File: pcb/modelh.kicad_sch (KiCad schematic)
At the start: 41 parts, among them J1 Battery Conn, J2 Conn_01x20, J3 Conn_01x06, J4 Conn_01x12, J5 Conn_01x04, SW1 SW_reset, U1 nice_nano, U2 74HC595, U3 74HC595, U4 74HC595

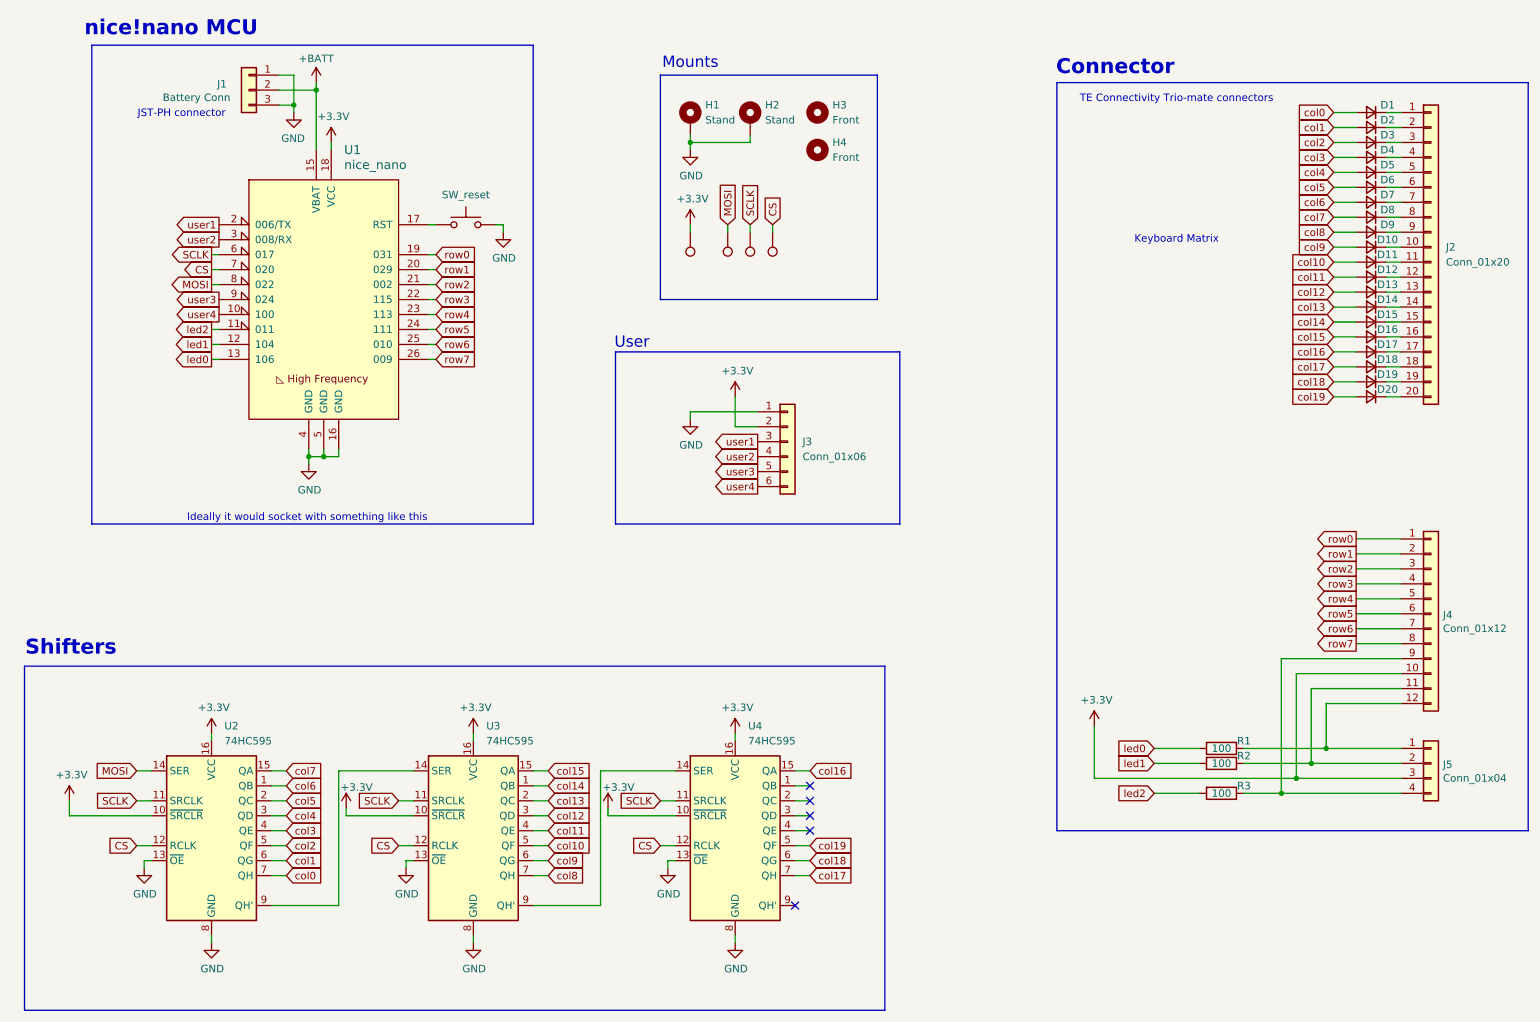
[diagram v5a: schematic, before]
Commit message: Aligned connectors correctly, added second 4 pin footprint
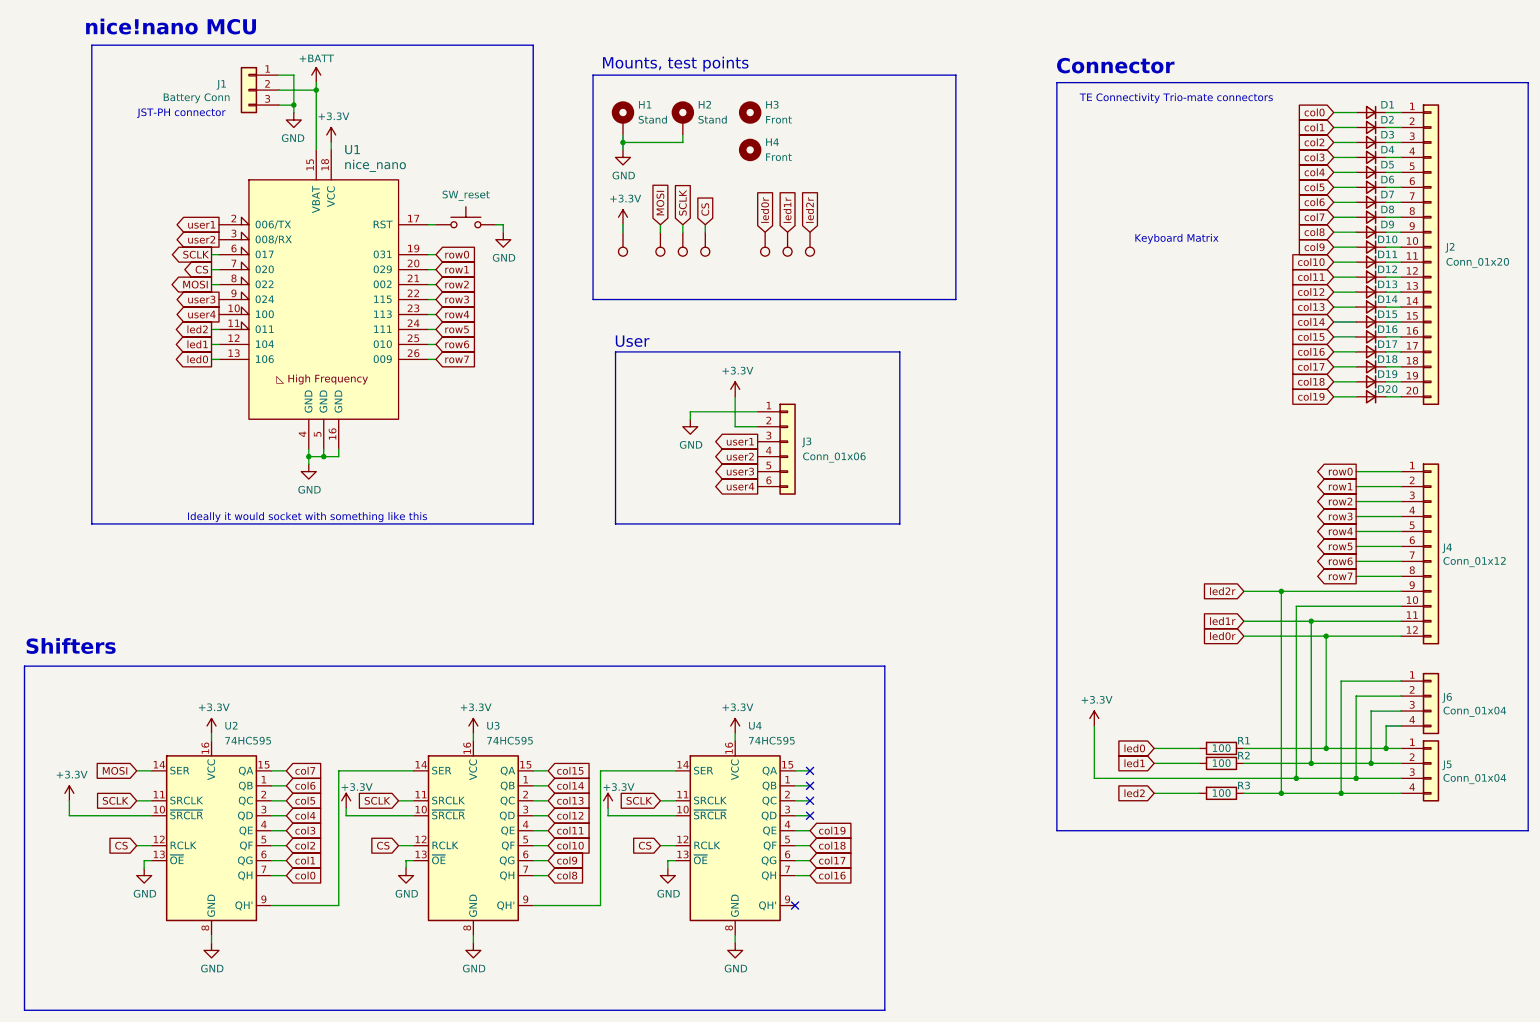
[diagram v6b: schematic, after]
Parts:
- added J6: Conn_01x04, Library:ModelH-triomate-leds4, symbol Connector_Generic:Conn_01x04
- added TP5: LED1, Library:TestPoint, symbol Connector:TestPoint
- added TP6: LED2, Library:TestPoint, symbol Connector:TestPoint
- added TP7: LED3, Library:TestPoint, symbol Connector:TestPoint
- D1, D10, D11, D12, D13, D14, D15, D16, D17, D18, D19, D2, D20, D3, D4, D5, D6, D7, D8, D9: footprint Diode_SMD:D_SOD-123F -> Library:DO-35 smaller
- J1: footprint Connector_JST:JST_PH_S3B-PH-K_1x03_P2.00mm_Horizontal -> Connector_JST:JST_PH_B3B-PH-K_1x03_P2.00mm_Vertical
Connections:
- net +3.3V: now also J6.2 (Pin_2)
- net GND: now also SW1.1; no longer SW1.2
- net col16: now also U4.7 (QH); no longer U4.15 (QA)
- net col17: now also U4.6 (QG); no longer U4.7 (QH)
- net col18: now also U4.5 (QF); no longer U4.6 (QG)
- net col19: now also U4.4 (QE); no longer U4.5 (QF)
- net led0r: now reaches J4.12 (Pin_12), J5.1 (Pin_1), R1.1
- net led0r: now also J6.4 (Pin_4), TP5.1
- net led1r: now reaches J4.11 (Pin_11), J5.2 (Pin_2), R2.1
- net led1r: now also J6.3 (Pin_3), TP6.1
- net led2r: now reaches J4.9 (Pin_9), J5.4 (Pin_4), R3.1
- net led2r: now also J6.1 (Pin_1), TP7.1
- net at U1.17 (RST): now also SW1.2; no longer SW1.1
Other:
- note added: "Mounts, test points"
- note removed: "Mounts"
- moved on the sheet: H1, H2, H3, H4, J4

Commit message: Added testpad labels, ibom
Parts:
- TP5: value LED1 -> LED0
- TP6: value LED2 -> LED1
- TP7: value LED3 -> LED2
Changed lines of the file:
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@@
 			)
 		)
-		(property "Datasheet" "~"
+		(property "Datasheet" "https://42keebs.eu/shop/parts/components/reset-switch/?attribute_type=Through-hole%202-pin%206x3&attribute_pa_colour=black"
 			(at 96.52 52.07 0)
 			(effects
@@
 			)
 		)
-		(property "Value" "LED2"
+		(property "Value" "LED1"
 			(at 148.59 67.564 0)
 			(effects
@@
 			)
 		)
-		(property "Value" "LED1"
+		(property "Value" "LED0"
 			(at 145.288 65.532 0)
 			(effects
@@
 			)
 		)
-		(property "Value" "LED3"
+		(property "Value" "LED2"
 			(at 153.67 65.786 0)
 			(effects

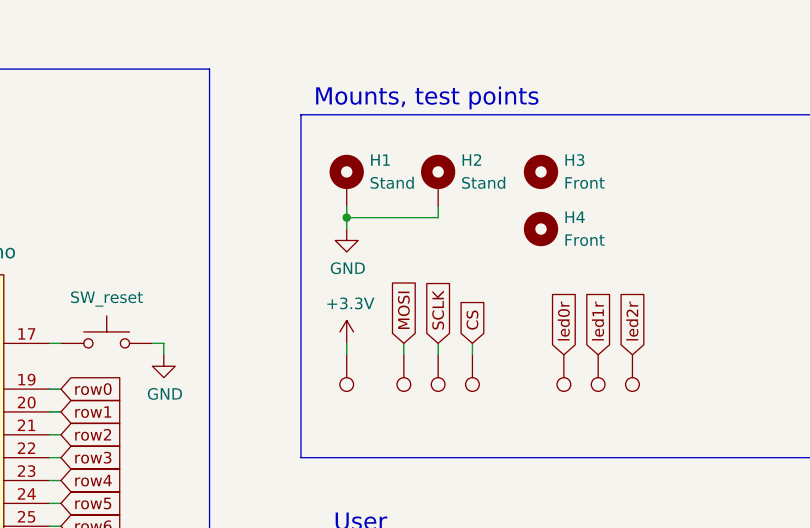
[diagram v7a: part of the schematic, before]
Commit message: Added third hole for M122
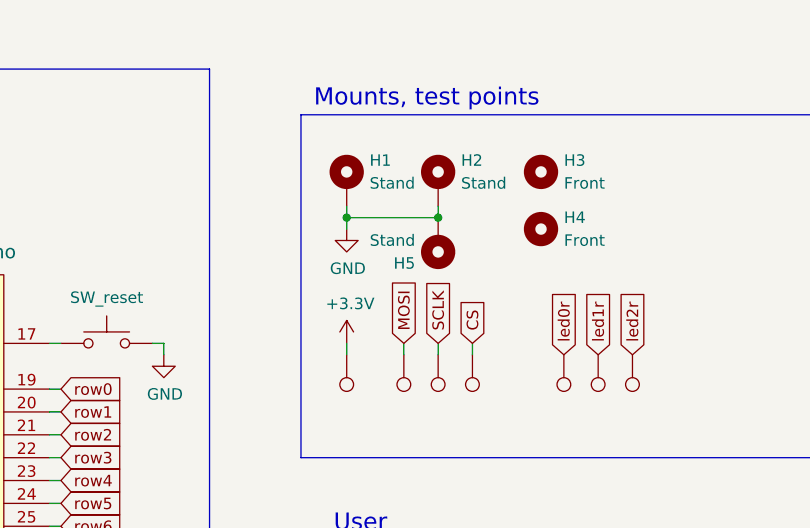
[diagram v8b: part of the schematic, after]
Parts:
- added H5: Stand, MountingHole:MountingHole_4mm_Pad_Via, symbol Mechanical:MountingHole_Pad
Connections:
- net GND: now also H5.1
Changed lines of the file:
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@@
 	)
 	(junction
+		(at 133.35 43.18)
+		(diameter 0)
+		(color 0 0 0 0)
+	)
+	(junction
 		(at 242.57 127)
 		(diameter 0)
@@
 					(unit 1)
 				)
+			)
+		)
+	)
+	(symbol
+		(lib_id "Mechanical:MountingHole_Pad")
+		(at 133.35 45.72 180)
+		(unit 1)
+		(exclude_from_sim yes)
+		(in_bom no)
+		(on_board yes)
+		(dnp no)
+		(property "Reference" "H5"
+			(at 130.81 48.2601 0)
+			(effects
+				(font
+					(size 1.27 1.27)
+				)
+				(justify left)
+			)
+		)
+		(property "Value" "Stand"
+			(at 130.81 45.7201 0)
+			(effects
+				(font
+					(size 1.27 1.27)
+				)
+				(justify left)
+			)
+		)
+		(property "Footprint" "MountingHole:MountingHole_4mm_Pad_Via"
+			(at 133.35 45.72 0)
+			(effects
+				(font
+					(size 1.27 1.27)
+				)
+				(hide yes)
+			)
+		)
+		(property "Datasheet" "~"
+			(at 133.35 45.72 0)
+			(effects
+				(font
+					(size 1.27 1.27)
+				)
+				(hide yes)
+			)
+		)
+		(property "Description" "Mounting Hole with connection"
+			(at 133.35 45.72 0)
+			(effects
+				(font
+					(size 1.27 1.27)
+				)
+				(hide yes)
+			)
+		)
+		(pin "1"
+		)
+		(instances
+			(project "modelh"
+				(path "/076b8a3b-b6a5-43e0-869d-187fc0ef2c0c"
+					(reference "H5")
+					(unit 1)
+				)
